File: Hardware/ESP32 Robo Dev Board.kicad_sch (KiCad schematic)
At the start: 23 parts, among them J1 PRG, U1 ESP32-S3-WROOM-1, U2 TCA9548ARGER, U3 AMS1117-3.3

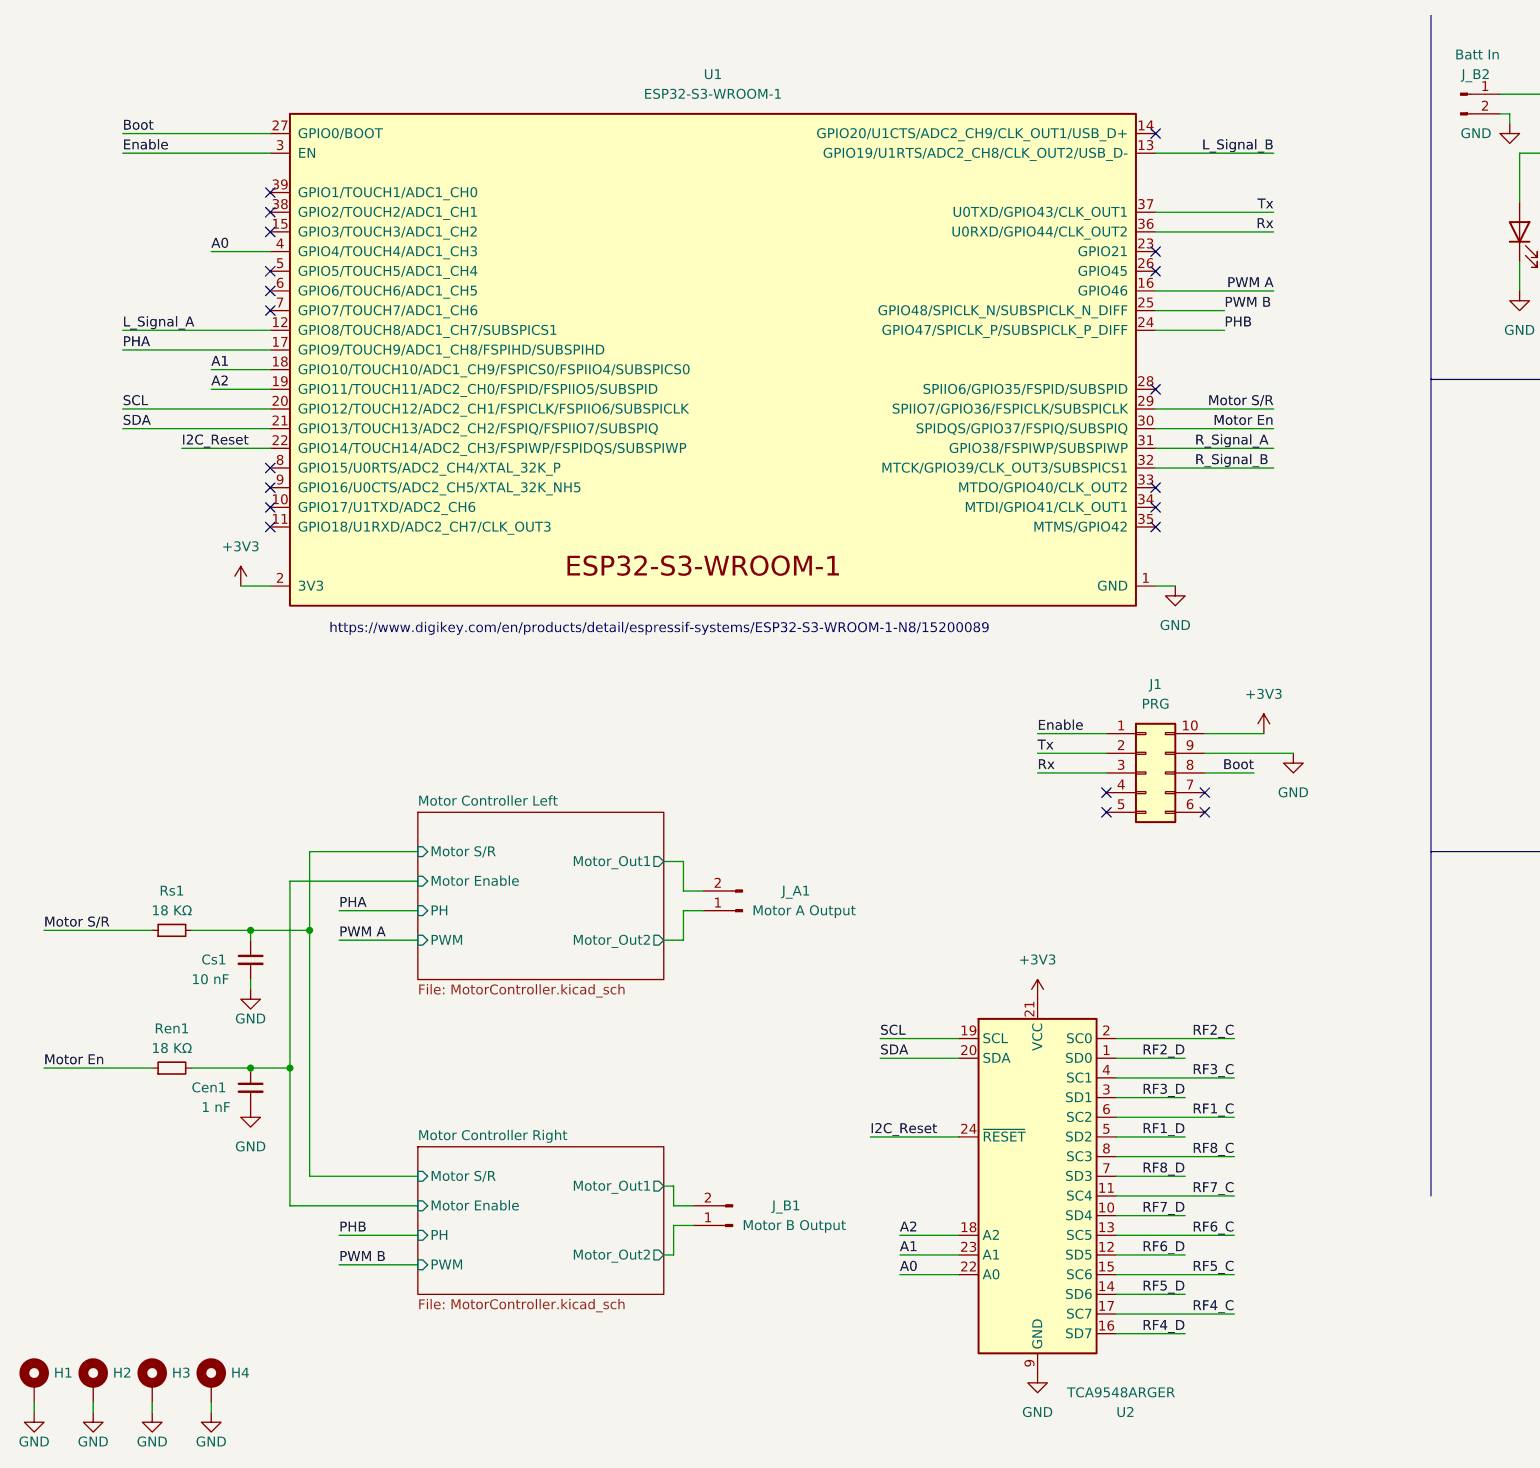
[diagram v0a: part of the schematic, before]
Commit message: Add USB C in Schematic
Added USB C support in sch not on PCB yet
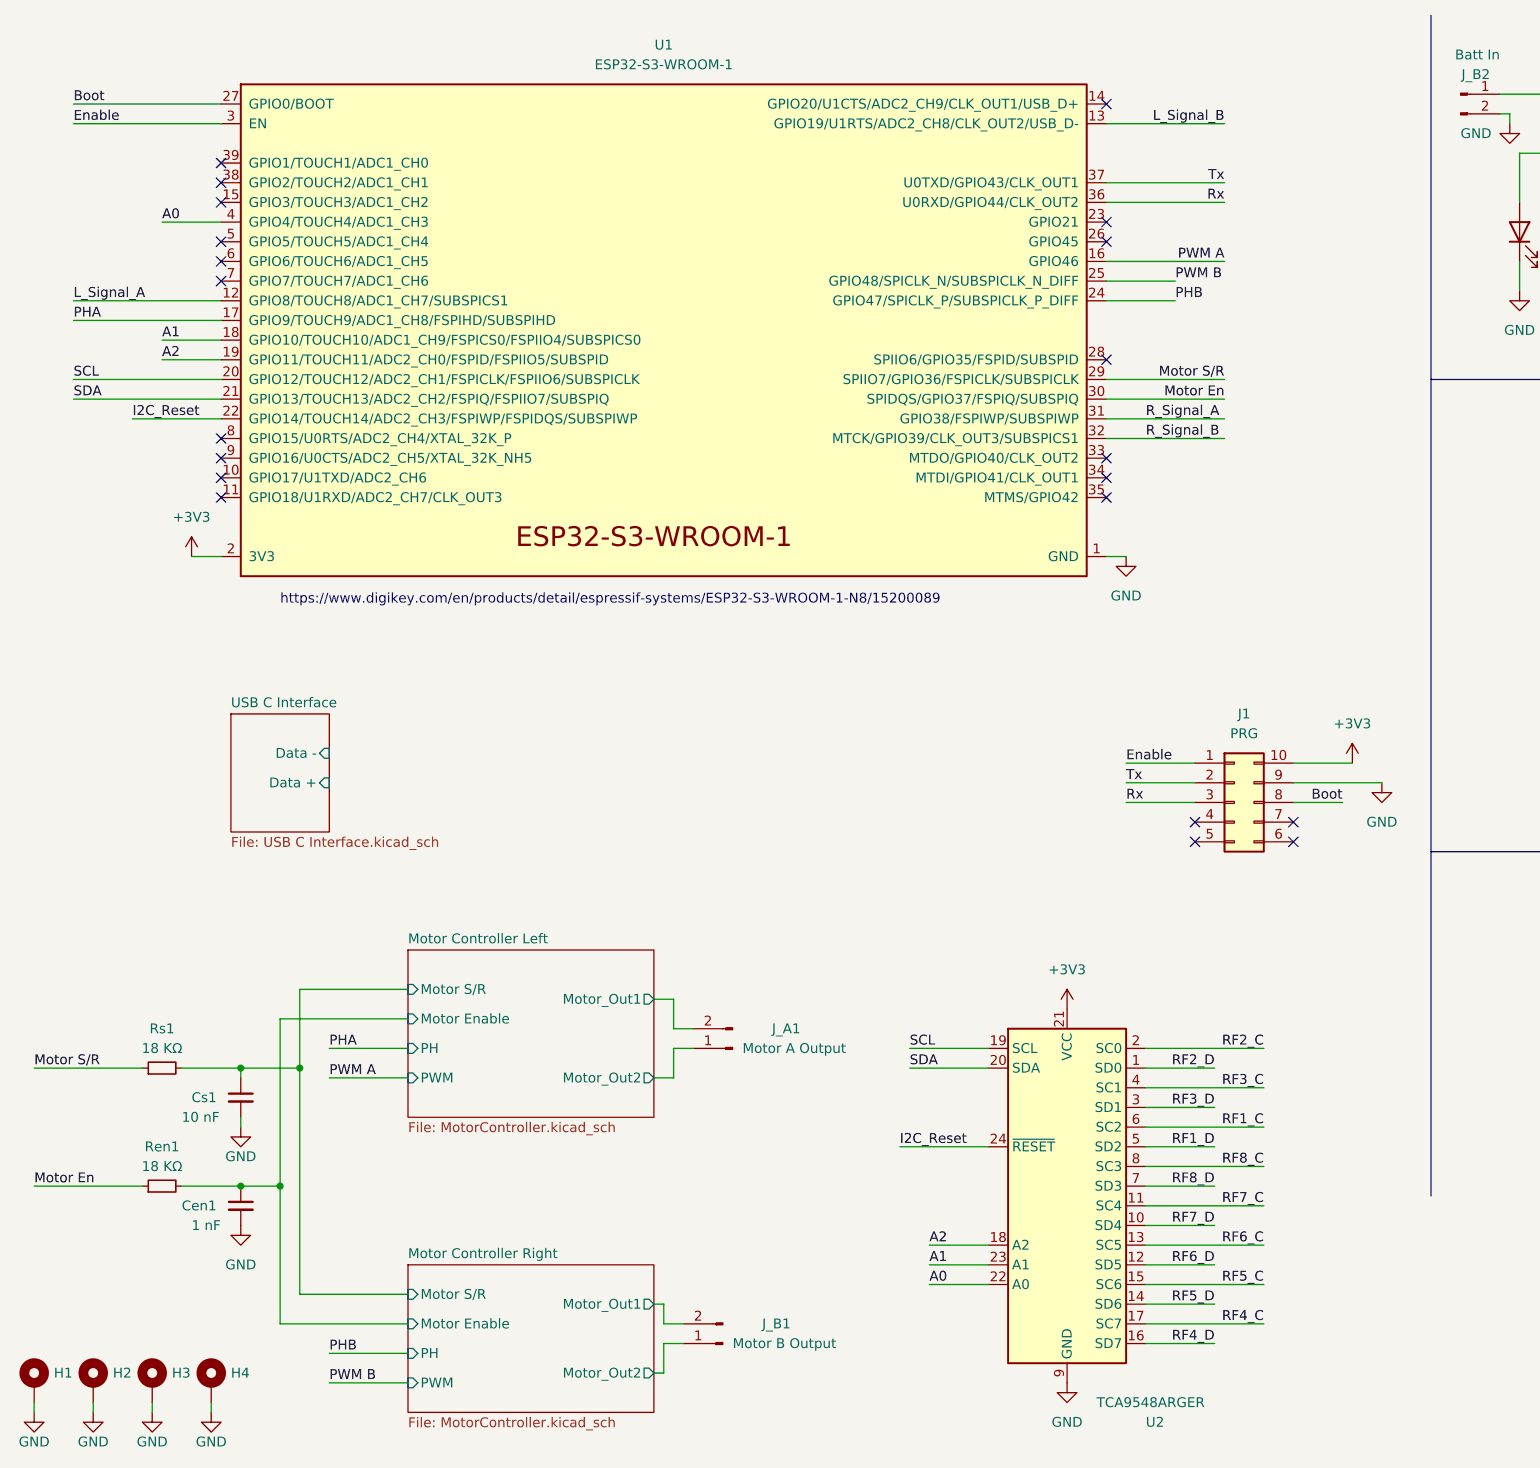
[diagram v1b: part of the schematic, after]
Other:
- added sheet USB C Interface (USB C Interface.kicad_sch)
- moved on the sheet: Cen1, Cs1, J1, J_A1, J_B1, Ren1, Rs1, U1, U2

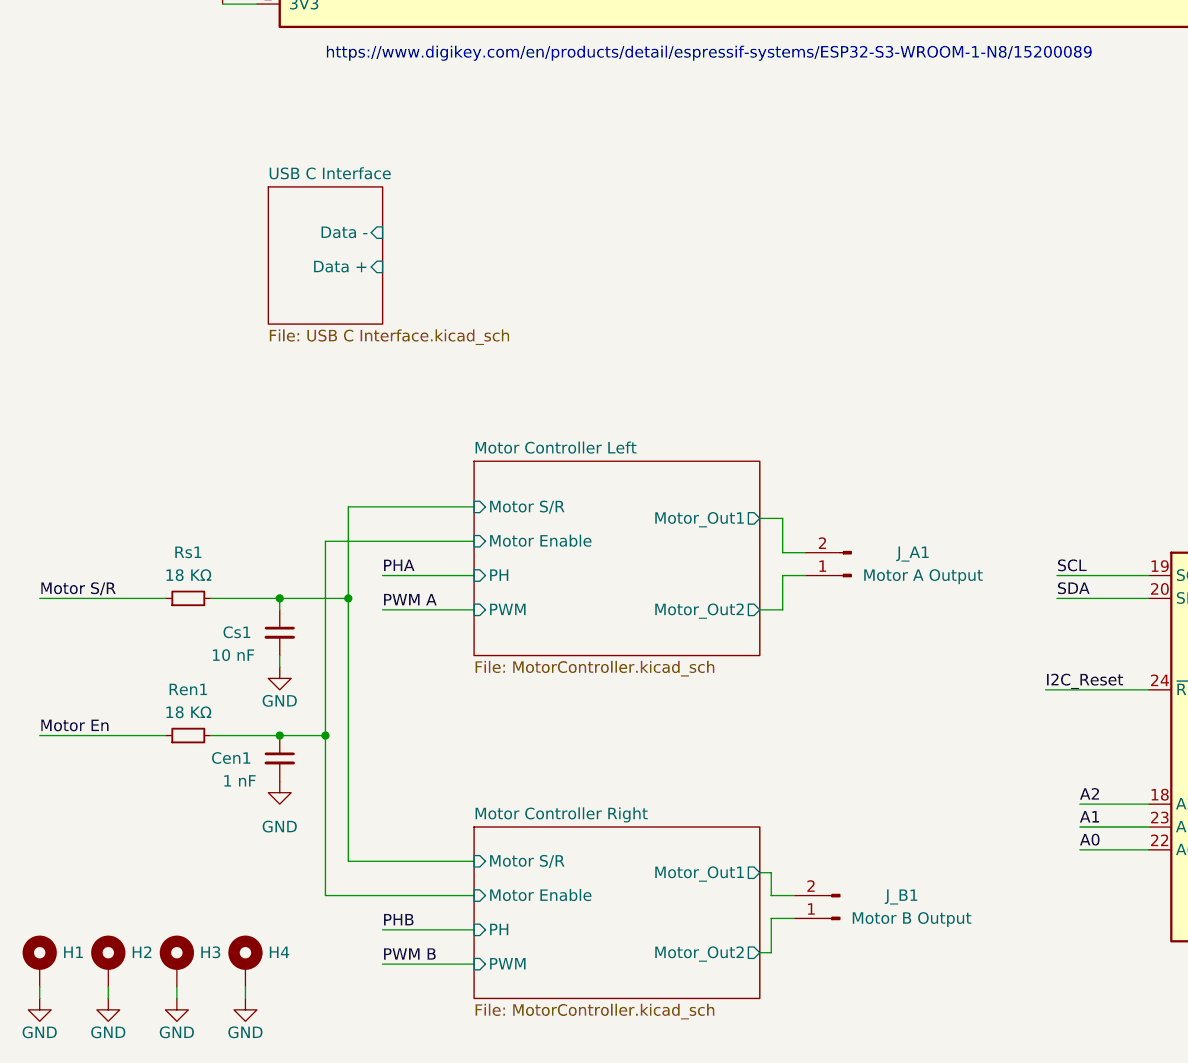
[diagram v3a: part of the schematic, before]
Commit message: Remove USB-C
USB C needs 4 layer for this. Remove now, profit later.
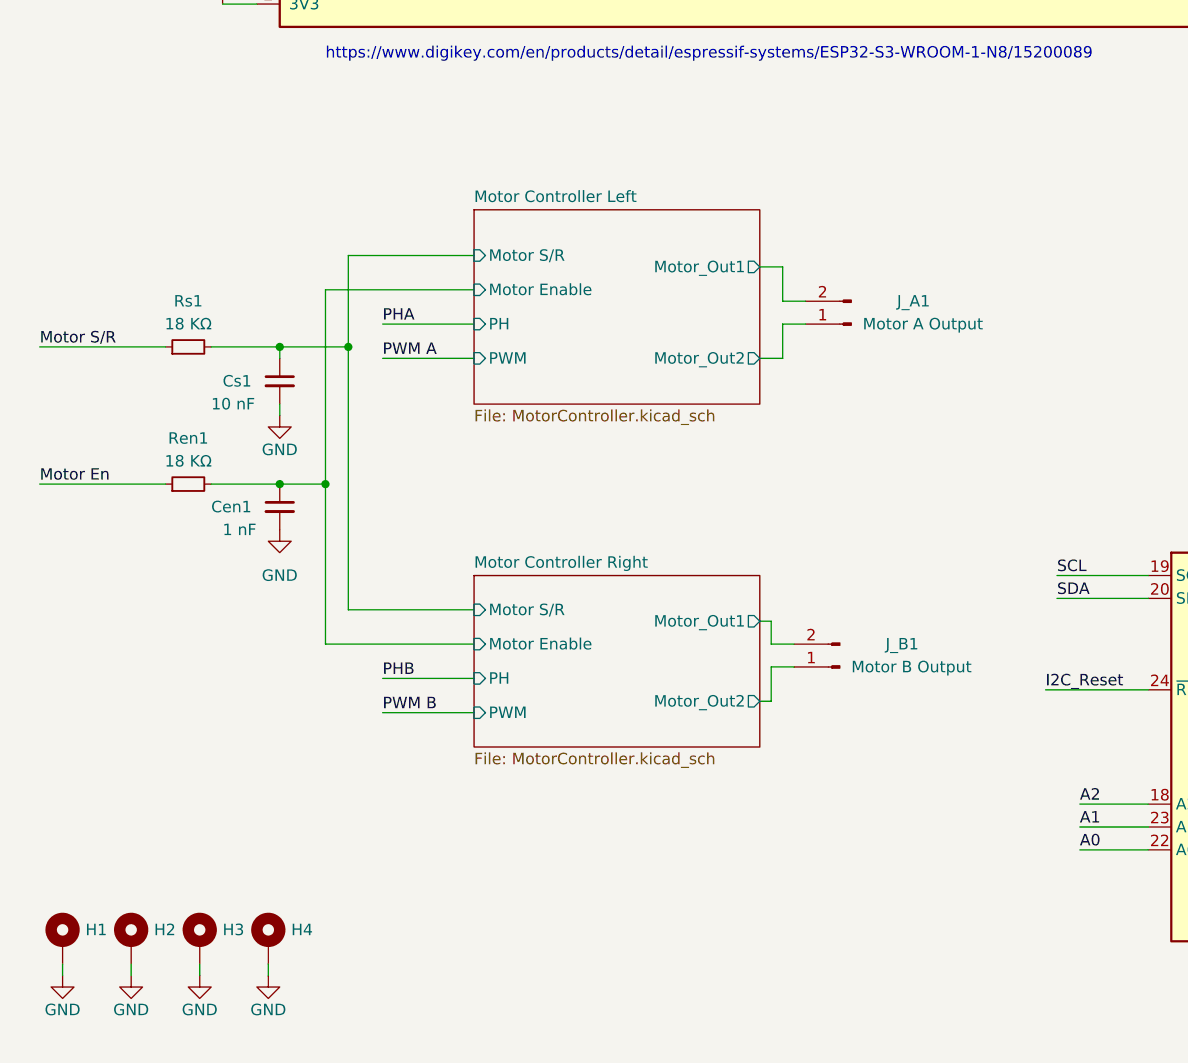
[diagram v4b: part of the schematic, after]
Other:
- removed sheet USB C Interface
- moved on the sheet: Cen1, Cs1, H1, H2, H3, H4, J_A1, J_B1, Ren1, Rs1

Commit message: Squashed commit of the following:
commit e6d18f1838a18780ff985c290e2821e2ac438ddc
Author: KenwoodFox <kenwood364@gmail.com>
Date:   Sun Oct 5 18:23:23 2025 -0400

    Tweaked n' fixed things with @Amoskeag

commit 133f082a76a13551d058af83ac953c852f82cbfb
Author: Arthur Aznive <61330561+Amoskeag@users.noreply.github.com>
Date:   Sun Oct 5 10:51:39 2025 -0400

    Update I2C Bus Connections

    Channel 4 of I2C was not connected, will make traces pretty later.

commit 1fc084a3994e8cc2965589d6eb11268a7396225d
Author: Arthur Aznive <61330561+Amoskeag@users.noreply.github.com>
Date:   Sun Oct 5 10:36:15 2025 -0400

    Board Refactor, Updated Parts

    Updated Board layout and added new parts

commit 6f7fc722645cc0153b695158322b161c2f880b4a
Author: Arthur Aznive <61330561+Amoskeag@users.noreply.github.com>
Date:   Fri Oct 3 23:22:42 2025 -0400

    update 2025

    board refactor

commit 2a13c54343b839d82b0e646e49a68070081abc7a
Author: Arthur Aznive <61330561+Amoskeag@users.noreply.github.com>
Date:   Fri Oct 3 23:04:47 2025 -0400

    Square Board Time

    Rerouting, restarting project, trying to make a simpler dev board. Lets see what we can do.

commit d4ab96b311134bb0a7992d948496d7b671a058de
Author: Arthur Aznive <61330561+Amoskeag@users.noreply.github.com>
Date:   Wed Jan 15 14:01:24 2025 -0500

    4 L:ayer Board with USB-C

    Created a 4-Layer PCB with USB-C updates

commit 55621a658c07626f43cd5cc55c172a27abc51e41
Author: Arthur Aznive <61330561+Amoskeag@users.noreply.github.com>
Date:   Tue Mar 5 00:57:37 2024 -0500

    Updated Motor Driver Routing

    Working on Power Supply and Motor Controller Routing

commit 3f2874cc29094c27990d838de84f4fea139067e1
Author: Arthur Aznive <61330561+Amoskeag@users.noreply.github.com>
Date:   Sun Mar 3 23:13:56 2024 -0500

    BIG Changes

    Create a 4 Layer Variation
    Change Motor Controller routing.
    Change Power Regulation.
    Optimize Sensor routing.
    Pray I know what i'm doing

commit 08b48da4672d4d2e9f554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
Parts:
- removed D1, D2: LED, Resistor_SMD:R_0805_2012Metric, symbol Device:LED
- removed E1: Encoder_L, Amoskeag_KiCAD_Lib:Kailh Encoder 9mm, symbol Amoskeag-KiCAD-Lib:Kailh_Encoder
- removed E2: Encoder_R, Amoskeag_KiCAD_Lib:Kailh Encoder 9mm, symbol Amoskeag-KiCAD-Lib:Kailh_Encoder
- removed H3, H4: MountingHole_Pad, MountingHole:MountingHole_2.2mm_M2_DIN965_Pad, symbol Mechanical:MountingHole_Pad
- removed J1: PRG, Connector:Tag-Connect_TC2050-IDC-FP_2x05_P1.27mm_Vertical, symbol Connector_Generic:Conn_02x05_Counter_Clockwise
- removed J_B2: Batt In, Connector_JST:JST_EH_B2B-EH-A_1x02_P2.50mm_Vertical, symbol Connector:Conn_01x02_Male
- removed U3: AMS1117-3.3, Package_TO_SOT_SMD:SOT-223-3_TabPin2, symbol Regulator_Linear:AMS1117-3.3
- added C10: 10 uF, Capacitor_SMD:C_0805_2012Metric, symbol Device:C_Small
- added C11: 1 uF, Capacitor_SMD:C_0805_2012Metric, symbol Device:C_Small
- added C5: 1uF, Capacitor_SMD:C_0805_2012Metric, symbol Device:C_Small
- added D2: 1N4448WT, Diode_SMD:D_SOD-523, symbol Diode:1N4448WT
- added D3: LED, Resistor_SMD:R_0805_2012Metric, symbol Device:LED
- added J10, J3, J4, J5, J6, J7, J8, J9: ~, Connector_PinHeader_1.00mm:PinHeader_1x04_P1.00mm_Vertical, symbol Connector:Conn_01x04_Pin
- added J2: Conn_01x02_Pin, Connector_PinHeader_1.27mm:PinHeader_1x02_P1.27mm_Vertical, symbol Connector:Conn_01x02_Pin
- added LED1: RED LED, LED_SMD:LED_0805_2012Metric, symbol Device:LED
- added Q1: DMP2045U, Package_TO_SOT_SMD:SOT-23, symbol Transistor_FET:NTR2101P
- added R10: 10k, Resistor_SMD:R_0805_2012Metric, symbol Device:R_Small
- added R4: 5.1k, Resistor_SMD:R_0805_2012Metric_Pad1.20x1.40mm_HandSolder, symbol Device:R_Small
- added R6: 5.1k, Resistor_SMD:R_0805_2012Metric, symbol Device:R_Small
- added R7, R8: 200k, Resistor_SMD:R_0805_2012Metric, symbol Device:R_Small
- added R9: 100k, Resistor_SMD:R_0805_2012Metric, symbol Device:R_Small
- added Rs2: 18 KΩ, Resistor_SMD:R_0603_1608Metric, symbol Device:R_Small
- added Rs3: 100, Resistor_SMD:R_0603_1608Metric, symbol Device:R_Small
- added SW1: SW_Push_Dual_x2, Button_Switch_SMD:SW_Push_SPST_NO_Alps_SKRK, symbol Switch:SW_Push_Dual_x2
- added SW2: SW_Push, Button_Switch_THT:SW_TH_Tactile_Omron_B3F-100x, symbol Switch:SW_Push
- added TP1, TP2, TP3, TP4, TP5: TestPoint, TestPoint:TestPoint_Pad_D1.0mm, symbol Connector:TestPoint
- added U8: MCP73831-2-OT, Package_TO_SOT_SMD:SOT-23-5, symbol Battery_Management:MCP73831-2-OT
- added U9: AP2112K-3.3, Package_TO_SOT_SMD:SOT-23-5, symbol Regulator_Linear:AP2112K-3.3
- C1: value 2.2 µF -> 10 µF; footprint Capacitor_SMD:C_0805_2012Metric -> Capacitor_SMD:C_1206_3216Metric_Pad1.33x1.80mm_HandSolder
- C2: value 2.2 µF -> 1 µF
- Cen1, Cs1: footprint Capacitor_SMD:C_0805_2012Metric -> Capacitor_SMD:C_0603_1608Metric
- R1: value 2K -> 5.1k
- R2: value 2K -> 100k
- Ren1, Rs1: footprint Resistor_SMD:R_0805_2012Metric -> Resistor_SMD:R_0603_1608Metric
- U2: footprint Package_DFN_QFN:Texas_RGE0024C_EP2.1x2.1mm -> Package_SO:TSSOP-24_4.4x7.8mm_P0.65mm
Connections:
- net +3V3: now also J10.4 (Pin_4), J3.4 (Pin_4), J4.4 (Pin_4), J5.4 (Pin_4), J6.4 (Pin_4), J7.4 (Pin_4), J8.4 (Pin_4), J9.4 (Pin_4), Rs3.2, TP1.1, U9.5 (VOUT); no longer R2.2
- net Boot: now also Rs2.2, SW2.2
- net GND: now also U2.18 (A2), U2.22 (A0), U2.23 (A1), C10.2, C11.2, C5.2, J10.1 (Pin_1), J2.1 (Pin_1), J3.1 (Pin_1), J4.1 (Pin_1), J5.1 (Pin_1), J6.1 (Pin_1), J7.1 (Pin_1), J8.1 (Pin_1), J9.1 (Pin_1), LED1.1 (K), R6.1, R8.2, R9.2, Rs2.1, SW1.1 (C), TP5.1, U8.2 (V_{SS}), U9.2 (GND)
- net L_Signal_B: now also U1.4 (GPIO4/TOUCH4/ADC1_CH3); no longer U1.13 (GPIO19/U1RTS/ADC2_CH8/CLK_OUT2/USB_D-)
- net PHA: now also U1.16 (GPIO46); no longer U1.17 (GPIO9/TOUCH9/ADC1_CH8/FSPIHD/SUBSPIHD)
- net PHB: now also U1.25 (GPIO48/SPICLK_N/SUBSPICLK_N_DIFF); no longer U1.24 (GPIO47/SPICLK_P/SUBSPICLK_P_DIFF)
- net PWM A: now also U1.17 (GPIO9/TOUCH9/ADC1_CH8/FSPIHD/SUBSPIHD); no longer U1.16 (GPIO46)
- net PWM B: now also U1.24 (GPIO47/SPICLK_P/SUBSPICLK_P_DIFF); no longer U1.25 (GPIO48/SPICLK_N/SUBSPICLK_N_DIFF)
- net R_Signal_A: now also U1.32 (MTCK/GPIO39/CLK_OUT3/SUBSPICS1); no longer U1.31 (GPIO38/FSPIWP/SUBSPIWP)
- net R_Signal_B: now also U1.31 (GPIO38/FSPIWP/SUBSPIWP); no longer U1.32 (MTCK/GPIO39/CLK_OUT3/SUBSPICS1)
- net at R1.2: now also U8.1 (STAT); no longer C1.1
- net V_IN: now reaches R2.1
- net V_IN: now also C1.1, D2.1 (K), Q1.2 (S), TP4.1, U9.1 (VIN)
- net at R1.1: now also D3.1 (K)
- net D+: now reaches U1.14 (GPIO20/U1CTS/ADC2_CH9/CLK_OUT1/USB_D+)
- net VBAT_DET: now reaches U1.28 (SPIIO6/GPIO35/FSPID/SUBSPID)
- net VBAT_DET: now also C11.1, R7.2, R8.1
- net GPIO1: now reaches U1.39 (GPIO1/TOUCH1/ADC1_CH0)
- net GPIO1: now also R4.1
- removed net A0: U1.4 (GPIO4/TOUCH4/ADC1_CH3), U2.22 (A0)
- net A1: no longer names the net of U1.18 (GPIO10/TOUCH10/ADC1_CH9/FSPICS0/FSPIIO4/SUBSPICS0)
- net A1: no longer U2.23 (A1)
- net A2: no longer names the net of U1.19 (GPIO11/TOUCH11/ADC2_CH0/FSPID/FSPIIO5/SUBSPID)
- net A2: no longer U2.18 (A2)
- net Enable renamed ~{RESET}
- net ~{RESET}: now also R10.1
- net RF1_C renamed I2C_2C
- net I2C_2C: now also J5.3 (Pin_3)
- net RF1_D renamed I2C_2D
- net I2C_2D: now also J5.2 (Pin_2)
- net RF2_C renamed I2C_0C
- net I2C_0C: now also J3.3 (Pin_3)
- net RF2_D renamed I2C_0D
- net I2C_0D: now also J3.2 (Pin_2)
- net RF3_C renamed I2C_1C
- net I2C_1C: now also J4.3 (Pin_3)
- net RF3_D renamed I2C_1D
- net I2C_1D: now also J4.2 (Pin_2)
- net RF4_C renamed I2C_7C
- net I2C_7C: now also J10.3 (Pin_3)
- net RF4_D renamed I2C_7D
- net I2C_7D: now also J10.2 (Pin_2)
- net RF5_C renamed I2C_6C
- net I2C_6C: now also J9.3 (Pin_3)
- net RF5_D renamed I2C_6D
- net I2C_6D: now also J9.2 (Pin_2)
- net RF6_C renamed I2C_5C
- net I2C_5C: now also J8.3 (Pin_3)
- net RF6_D renamed I2C_5D
- net I2C_5D: now also J8.2 (Pin_2)
- net RF7_C renamed I2C_4C
- net I2C_4C: now also J7.3 (Pin_3)
- net RF7_D renamed I2C_4D
- net I2C_4D: now also J7.2 (Pin_2)
- net RF8_C renamed I2C_3C
- net I2C_3C: now also J6.3 (Pin_3)
- net RF8_D renamed I2C_3D
- net I2C_3D: now also J6.2 (Pin_2)
- net Rx: no longer names the net of U1.36 (U0RXD/GPIO44/CLK_OUT2)
- net Tx: no longer names the net of U1.37 (U0TXD/GPIO43/CLK_OUT1)
- new net: C5.1, R10.2, SW1.2 (D)
- new net: R6.2, U8.5 (PROG)
- new net: R2.2, U9.3 (EN)
- new net: Rs3.1, SW2.1
- new net: LED1.2 (A), R4.2
- new net D-: U1.13 (GPIO19/U1RTS/ADC2_CH8/CLK_OUT2/USB_D-)
- new net V_BAT: C10.1, J2.2 (Pin_2), Q1.3 (D), R7.1, TP2.1, U8.3 (V_{BAT})
- new net V_BUS: D2.2 (A), D3.2 (A), Q1.1 (G), R9.1, TP3.1, U8.4 (V_{DD})
- no-connect marks 23 -> 18
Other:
- removed sheet Proximity Array
- added sheet USB C Interface (USB C Interface.kicad_sch)
- sheet Motor Controller Left ports: added V_BAT; removed none
- sheet Motor Controller Right ports: added V_BAT; removed none
- note added: "I2C Mux"
- note added: "LED Feedback"
- note added: "LiPO Charging"
- note added: "LiPO Monitor"
- note added: "MBR0540 Schottky Diode?"
- note added: "Might need a regulator that can pull more current. TLV76733DRVR"
- note added: "Motor Controls"
- note added: "Reset Circuts"
- note added: "Test Points"
- note added: "USB_C Interface should be easier to route without the extra components taking up room on the top layer. Questions: 1.) How to interface with ESP32: DONE 2.) How to charge Battery, DONE 3.) Disable robot motors when connected to USB? TBD"
- note added: "You can read this pin's voltage, then double it, to get the battery voltage."
- note removed: "Left and Right Wheel Encoders"
- note removed: "TCRTL5000L Array"
- title: TurtleBot Mainboard -> RoboDojo Development Board
- moved on the sheet: C1, C2, Cen1, Cs1, H1, H2, J_A1, J_B1, Ren1, Rs1, U1, U2
